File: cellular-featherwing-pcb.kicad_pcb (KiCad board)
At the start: 2 copper layers, 54 x 27 mm, 69 parts, among them J1 SIM8060-6-0-14-00-A, J2 TSM-116-01-L-SV, J3 TSM-112-01-L-SV, J4 U.FL-R-SMT, U1 BG96, U2 TPS63020QDSJTQ1, U3 TXB0108DQSR, U4 MAX8868EUK30+T

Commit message: Small updates
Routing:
- net (no net): track 13.9 -> 0.00 mm
- net Net-(C6-Pad1): track 0.00 -> 8.50 mm
- net Net-(C1-Pad1): track 0.00 -> 6.68 mm
- net Net-(R1-Pad2): track 0.00 -> 4.43 mm
- net GPS_ANT: track 3.97 -> 0.00 mm
- net VIN: track 0.00 -> 2.40 mm
- net Net-(C4-Pad1): track 0.00 -> 1.46 mm
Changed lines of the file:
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@@
     (property "Sheetname" "")
     (attr through_hole)
-    (fp_text reference "J2" (at -17.145 4.825) (layer "B.SilkS")
+    (fp_text reference "J2" (at -17.145 4.825) (layer "B.SilkS") hide
       (effects (font (size 1 1) (thickness 0.15)) (justify mirror))
     )
-    (fp_text value "TSM-116-01-L-SV" (at -6.35 -4.805) (layer "B.Fab")
+    (fp_text value "TSM-116-01-L-SV" (at -6.35 -4.805) (layer "B.Fab") hide
       (effects (font (size 1 1) (thickness 0.15)) (justify mirror))
     )
@@
     (property "Sheetname" "")
     (attr through_hole)
-    (fp_text reference "U4" (at 0.032 2.2064 90) (layer "B.SilkS")
+    (fp_text reference "U4" (at 0.032 2.2064 90) (layer "B.SilkS") hide
       (effects (font (size 0.64 0.64) (thickness 0.15)) (justify mirror))
     )
-    (fp_text value "MAX8868EUK30+T" (at 4.5024 -2.1936 90) (layer "B.Fab")
+    (fp_text value "MAX8868EUK30+T" (at 4.5024 -2.1936 90) (layer "B.Fab") hide
       (effects (font (size 0.64 0.64) (thickness 0.15)) (justify mirror))
     )
@@
     (property "Sheetname" "")
     (attr through_hole)
-    (fp_text reference "J3" (at -12.065 4.825) (layer "B.SilkS")
+    (fp_text reference "J3" (at -12.065 4.825) (layer "B.SilkS") hide
       (effects (font (size 1 1) (thickness 0.15)) (justify mirror))
     )
-    (fp_text value "TSM-112-01-L-SV" (at -1.27 -4.805) (layer "B.Fab")
+    (fp_text value "TSM-112-01-L-SV" (at -1.27 -4.805) (layer "B.Fab") hide
       (effects (font (size 1 1) (thickness 0.15)) (justify mirror))
     )
@@
   )
   (gr_rect locked (start 121 108) (end 175 81) (layer "Edge.Cuts") (width 0.1) (fill none))
-  (segment (start 163.0875 104.87) (end 162.0625 104.87) (width 0.25) (layer "F.Cu") (net 0))
-  (segment (start 167.95 107.3) (end 162.3925 107.3) (width 0.25) (layer "F.Cu") (net 0))
-  (segment (start 167.8875 104.9) (end 168.8875 104.9) (width 0.25) (layer "F.Cu") (net 0))
-  (segment (start 162.0625 104.87) (end 161.7875 105.145) (width 0.25) (layer "F.Cu") (net 0))
-  (segment (start 168.8875 106.3625) (end 167.95 107.3) (width 0.25) (layer "F.Cu") (net 0))
-  (segment (start 168.8875 104.9) (end 169.8875 104.9) (width 0.25) (layer "F.Cu") (net 0))
-  (segment (start 169.8875 104.9) (end 171.2 104.9) (width 0.25) (layer "F.Cu") (net 0))
-  (segment (start 162.3925 107.3) (end 161.7875 106.695) (width 0.25) (layer "F.Cu") (net 0))
-  (segment (start 166.9175 104.9) (end 167.8875 104.9) (width 0.25) (layer "F.Cu") (net 0))
-  (segment (start 168.8875 105.87) (end 168.8875 106.3625) (width 0.25) (layer "F.Cu") (net 0))
   (segment (start 170.78 97.95) (end 170.78 99.385) (width 0.2) (layer "B.Cu") (net 16))
   (segment (start 170.78 99.385) (end 170.8 99.405) (width 0.2) (layer "B.Cu") (net 16))
@@
   (segment (start 134.38 98.76) (end 134.38 97.205) (width 0.25) (layer "F.Cu") (net 73))
   (segment (start 134.38 97.205) (end 134.375 97.2) (width 0.25) (layer "F.Cu") (net 73))
-  (segment (start 165 104.8825) (end 165.0175 104.9) (width 0.25) (layer "F.Cu") (net 77))
-  (segment (start 165 101.88) (end 165 104.8825) (width 0.25) (layer "F.Cu") (net 77))
-  (segment (start 165.0175 104.9) (end 165.9575 104.9) (width 0.25) (layer "F.Cu") (net 77))
   (segment (start 169.35 87.45) (end 170.29 87.45) (width 0.25) (layer "F.Cu") (net 79))
   (segment (start 166.33 87.45) (end 169.35 87.45) (width 0.25) (layer "F.Cu") (net 79))
+  (segment (start 157.105 92.425) (end 156.95 92.27) (width 0.25) (layer "B.Cu") (net 81))
+  (segment (start 156.95 92.27) (end 155.8925 92.27) (width 0.25) (layer "B.Cu") (net 81))
+  (segment (start 155.6625 93.5375) (end 155.6625 92.5) (width 0.25) (layer "B.Cu") (net 81))
+  (segment (start 154.51 94) (end 155.2 94) (width 0.25) (layer "B.Cu") (net 81))
+  (segment (start 155.8925 92.27) (end 155.6625 92.5) (width 0.25) (layer "B.Cu") (net 81))
+  (segment (start 158.25 92.425) (end 157.105 92.425) (width 0.25) (layer "B.Cu") (net 81))
+  (segment (start 155.2 94) (end 155.6625 93.5375) (width 0.25) (layer "B.Cu") (net 81))
+  (segment (start 159.8 92.425) (end 158.25 92.425) (width 0.25) (layer "B.Cu") (net 81))
+  (segment (start 164.3875 90.7) (end 164.72 90.7) (width 0.25) (layer "B.Cu") (net 82))
+  (segment (start 164.72 90.7) (end 165.52 89.9) (width 0.25) (layer "B.Cu") (net 82))
+  (segment (start 167.75 92.425) (end 166.2 92.425) (width 0.25) (layer "B.Cu") (net 83))
+  (segment (start 164.3875 92.7) (end 164.3875 92.2) (width 0.25) (layer "B.Cu") (net 83))
+  (segment (start 169.3 92.425) (end 167.75 92.425) (width 0.25) (layer "B.Cu") (net 83))
+  (segment (start 164.3875 92.2) (end 165.975 92.2) (width 0.25) (layer "B.Cu") (net 83))
+  (segment (start 169.61 92.115) (end 169.3 92.425) (width 0.25) (layer "B.Cu") (net 83))
+  (segment (start 170.8875 92.425) (end 169.3 92.425) (width 0.25) (layer "B.Cu") (net 83))
+  (segment (start 169.61 91.15) (end 169.61 92.115) (width 0.25) (layer "B.Cu") (net 83))
+  (segment (start 165.975 92.2) (end 166.2 92.425) (width 0.25) (layer "B.Cu") (net 83))
   (segment (start 172.25 86.4625) (end 172.25 85.0875) (width 0.25) (layer "F.Cu") (net 84))
   (segment (start 172.25 87.45) (end 172.25 86.4625) (width 0.25) (layer "F.Cu") (net 84))
@@
   (segment (start 127.88 97.345) (end 128.025 97.2) (width 0.25) (layer "F.Cu") (net 86))
   (segment (start 127.88 99.26) (end 127.88 97.345) (width 0.25) (layer "F.Cu") (net 86))
+  (segment (start 137.55 91.8) (end 139.95 91.8) (width 0.25) (layer "B.Cu") (net 87))
   (segment (start 133.08 98.76) (end 131.88 98.76) (width 0.25) (layer "F.Cu") (net 88))
   (segment (start 131.85 97.215) (end 131.835 97.2) (width 0.25) (layer "F.Cu") (net 88))
@@
   (segment (start 169.85 101.895) (end 168.515 101.895) (width 0.2) (layer "B.Cu") (net 90))
   (segment (start 168.515 101.895) (end 168.5 101.88) (width 0.2) (layer "B.Cu") (net 90))
+  (segment (start 168.59 91.15) (end 167.65 91.15) (width 0.25) (layer "B.Cu") (net 91))
+  (segment (start 167.65 91.15) (end 167.6 91.2) (width 0.25) (layer "B.Cu") (net 91))
+  (segment (start 165.5 91.2) (end 167.6 91.2) (width 0.25) (layer "B.Cu") (net 91))
+  (segment (start 165 91.7) (end 165.5 91.2) (width 0.25) (layer "B.Cu") (net 91))
+  (segment (start 164.3875 91.7) (end 165 91.7) (width 0.25) (layer "B.Cu") (net 91))
   (segment (start 161.5875 93.2) (end 161.5875 93.7) (width 0.2) (layer "B.Cu") (net 94))
   (zone (net 16) (net_name "GND") (layer "F.Cu") (hatch edge 0.508)

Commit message: Updates from Javier
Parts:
- removed C30, C31, C33: 4.7uF, Capacitor_SMD:C_0402_1005Metric
- removed U4: MAX8868EUK30+T, MAX8868EUK30_:SOT95P280X145-5N
- moved TP12 12.1 mm to (152.9, 101.4)
- moved TP6 10.2 mm to (139.1, 95.1)
- moved TP5 4.91 mm to (141.6, 93.5)
- moved TP4 2.34 mm to (145.5, 92.6)
- moved TP8 1.69 mm to (139.2, 97.4)
- moved C34 0.53 mm to (144.1, 93.6)
- moved TP9 0.43 mm to (159.5, 89.0)
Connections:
- U1 pad 102: GND -> (no net)
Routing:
- net Net-(U1-Pad11): track 0.00 -> 73.6 mm
- net VDD: track 0.00 -> 62.5 mm, vias 0 -> 1
- net SIM_VDD: track 1.56 -> 62.4 mm, vias 0 -> 3
- net SIM_CLK: track 0.00 -> 40.7 mm
- net SIM_DATA: track 0.00 -> 35.6 mm
- net VMODEM: track 1.47 -> 36.7 mm, vias 0 -> 2
- net SIM_RST: track 0.00 -> 32.2 mm
- net GND: track 2.95 -> 32.6 mm, vias 0 -> 18
- net Net-(C16-Pad1): track 2.12 -> 27.3 mm, vias 0 -> 2
- net GSM_RXD: track 0.00 -> 24.7 mm
- net ENABLE: track 0.00 -> 24.4 mm
- net GSM_TXD: track 0.00 -> 20.3 mm
- net RI: track 0.00 -> 19.0 mm, vias 0 -> 1
- net DCD: track 0.00 -> 18.7 mm, vias 0 -> 1
- net GSM_STATUS_INT: track 0.00 -> 17.6 mm, vias 0 -> 1
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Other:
- board size 54 x 27 mm -> 54 x 32 mm

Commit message: Updated board from javier
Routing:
- net GND: vias 18 -> 19
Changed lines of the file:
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@@
     (fp_line (start -1.5 2) (end 1.5 2) (layer "B.Fab") (width 0.127))
     (fp_circle (center -2.2 1.5) (end -2.1 1.5) (layer "B.Fab") (width 0.2) (fill none))
-    (pad "1" smd oval locked (at -1.4 1.5 180) (size 0.6 0.24) (layers "B.Cu" "B.Paste")
+    (pad "1" smd oval (at -1.4 1.5 180) (size 0.6 0.24) (layers "B.Cu" "B.Paste")
       (net 82 "Net-(C4-Pad1)") (pinfunction "VINA") (pintype "input"))
-    (pad "2" smd oval locked (at -1.4 1 180) (size 0.6 0.24) (layers "B.Cu" "B.Paste")
+    (pad "2" smd oval (at -1.4 1 180) (size 0.6 0.24) (layers "B.Cu" "B.Paste")
       (net 16 "GND") (pinfunction "GND") (pintype "power_in"))
-    (pad "3" smd oval locked (at -1.4 0.5 180) (size 0.6 0.24) (layers "B.Cu" "B.Paste")
+    (pad "3" smd oval (at -1.4 0.5 180) (size 0.6 0.24) (layers "B.Cu" "B.Paste")
       (net 90 "Net-(R1-Pad2)") (pinfunction "FB") (pintype "input"))
-    (pad "4" smd oval locked (at -1.4 0 180) (size 0.6 0.24) (layers "B.Cu" "B.Paste")
+    (pad "4" smd oval (at -1.4 0 180) (size 0.6 0.24) (layers "B.Cu" "B.Paste")
       (net 83 "Net-(C6-Pad1)") (pinfunction "VOUT_4") (pintype "output"))
-    (pad "5" smd oval locked (at -1.4 -0.5 180) (size 0.6 0.24) (layers "B.Cu" "B.Paste")
+    (pad "5" smd oval (at -1.4 -0.5 180) (size 0.6 0.24) (layers "B.Cu" "B.Paste")
       (net 83 "Net-(C6-Pad1)") (pinfunction "VOUT_5") (pintype "output"))
-    (pad "6" smd oval locked (at -1.4 -1 180) (size 0.6 0.24) (layers "B.Cu" "B.Paste")
+    (pad "6" smd oval (at -1.4 -1 180) (size 0.6 0.24) (layers "B.Cu" "B.Paste")
       (net 94 "/L1_1") (pinfunction "L2_6") (pintype "passive"))
-    (pad "7" smd oval locked (at -1.4 -1.5 180) (size 0.6 0.24) (layers "B.Cu" "B.Paste")
+    (pad "7" smd oval (at -1.4 -1.5 180) (size 0.6 0.24) (layers "B.Cu" "B.Paste")
       (net 94 "/L1_1") (pinfunction "L2_7") (pintype "passive"))
-    (pad "8" smd oval locked (at 1.4 -1.5 180) (size 0.6 0.24) (layers "B.Cu" "B.Paste")
+    (pad "8" smd oval (at 1.4 -1.5 180) (size 0.6 0.24) (layers "B.Cu" "B.Paste")
       (net 93 "/L1_2") (pinfunction "L1_8") (pintype "passive"))
-    (pad "9" smd oval locked (at 1.4 -1 180) (size 0.6 0.24) (layers "B.Cu" "B.Paste")
+    (pad "9" smd oval (at 1.4 -1 180) (size 0.6 0.24) (layers "B.Cu" "B.Paste")
       (net 93 "/L1_2") (pinfunction "L1_9") (pintype "passive"))
-    (pad "10" smd oval locked (at 1.4 -0.5 180) (size 0.6 0.24) (layers "B.Cu" "B.Paste")
+    (pad "10" smd oval (at 1.4 -0.5 180) (size 0.6 0.24) (layers "B.Cu" "B.Paste")
       (net 81 "Net-(C1-Pad1)") (pinfunction "VIN_10") (pintype "input"))
-    (pad "11" smd oval locked (at 1.4 0 180) (size 0.6 0.24) (layers "B.Cu" "B.Paste")
+    (pad "11" smd oval (at 1.4 0 180) (size 0.6 0.24) (layers "B.Cu" "B.Paste")
       (net 81 "Net-(C1-Pad1)") (pinfunction "VIN_11") (pintype "input"))
-    (pad "12" smd oval locked (at 1.4 0.5 180) (size 0.6 0.24) (layers "B.Cu" "B.Paste")
+    (pad "12" smd oval (at 1.4 0.5 180) (size 0.6 0.24) (layers "B.Cu" "B.Paste")
       (net 47 "ENABLE") (pinfunction "EN") (pintype "input"))
-    (pad "13" smd oval locked (at 1.4 1 180) (size 0.6 0.24) (layers "B.Cu" "B.Paste")
+    (pad "13" smd oval (at 1.4 1 180) (size 0.6 0.24) (layers "B.Cu" "B.Paste")
       (net 81 "Net-(C1-Pad1)") (pinfunction "PS/SYNC") (pintype "input"))
-    (pad "14" smd oval locked (at 1.4 1.5 180) (size 0.6 0.24) (layers "B.Cu" "B.Paste")
+    (pad "14" smd oval (at 1.4 1.5 180) (size 0.6 0.24) (layers "B.Cu" "B.Paste")
       (net 19 "unconnected-(U2-Pad14)") (pinfunction "PG") (pintype "output"))
-    (pad "15" smd custom locked (at 0 0 180) (size 1.5 2.8) (layers "B.Cu")
+    (pad "15" smd custom (at 0 0 180) (size 1.5 2.8) (layers "B.Cu")
       (net 16 "GND") (pinfunction "PGND") (pintype "power_in") (zone_connect 0)
       (options (clearance outline) (anchor rect))
@@
           ) (width 0.01) (fill yes))
       ))
-    (pad "16" thru_hole circle locked (at -0.5 1 180) (size 0.3 0.3) (drill 0.2) (layers *.Cu *.Mask))
-    (pad "17" thru_hole circle locked (at 0 1 180) (size 0.3 0.3) (drill 0.2) (layers *.Cu *.Mask))
-    (pad "18" thru_hole circle locked (at 0.5 1 180) (size 0.3 0.3) (drill 0.2) (layers *.Cu *.Mask))
-    (pad "19" thru_hole circle locked (at -0.5 0.5 180) (size 0.3 0.3) (drill 0.2) (layers *.Cu *.Mask))
-    (pad "20" thru_hole circle locked (at 0 0.5 180) (size 0.3 0.3) (drill 0.2) (layers *.Cu *.Mask))
-    (pad "21" thru_hole circle locked (at 0.5 0.5 180) (size 0.3 0.3) (drill 0.2) (layers *.Cu *.Mask))
-    (pad "22" thru_hole circle locked (at -0.5 0 180) (size 0.3 0.3) (drill 0.2) (layers *.Cu *.Mask))
-    (pad "23" thru_hole circle locked (at 0 0 180) (size 0.3 0.3) (drill 0.2) (layers *.Cu *.Mask))
-    (pad "24" thru_hole circle locked (at 0.5 0 180) (size 0.3 0.3) (drill 0.2) (layers *.Cu *.Mask))
-    (pad "25" thru_hole circle locked (at -0.5 -0.5 180) (size 0.3 0.3) (drill 0.2) (layers *.Cu *.Mask))
-    (pad "26" thru_hole circle locked (at 0 -0.5 180) (size 0.3 0.3) (drill 0.2) (layers *.Cu *.Mask))
-    (pad "27" thru_hole circle locked (at 0.5 -0.5 180) (size 0.3 0.3) (drill 0.2) (layers *.Cu *.Mask))
-    (pad "28" thru_hole circle locked (at -0.5 -1 180) (size 0.3 0.3) (drill 0.2) (layers *.Cu *.Mask))
-    (pad "29" thru_hole circle locked (at 0 -1 180) (size 0.3 0.3) (drill 0.2) (layers *.Cu *.Mask))
-    (pad "30" thru_hole circle locked (at 0.5 -1 180) (size 0.3 0.3) (drill 0.2) (layers *.Cu *.Mask))
   )
   (footprint "TestPoint:TestPoint_Pad_D1.0mm" (layer "B.Cu")
@@
   (via (at 132.969 100.5078) (size 0.8) (drill 0.4) (layers "F.Cu" "B.Cu") (free) (net 16))
   (via (at 151.7396 92.8624) (size 0.8) (drill 0.4) (layers "F.Cu" "B.Cu") (free) (net 16))
+  (via (at 162.941 91.8718) (size 0.8) (drill 0.4) (layers "F.Cu" "B.Cu") (net 16))
   (via (at 168.021 96.52) (size 0.8) (drill 0.4) (layers "F.Cu" "B.Cu") (free) (net 16))
   (via (at 138.9888 93.345) (size 0.8) (drill 0.4) (layers "F.Cu" "B.Cu") (net 16))
@@
   (via (at 161.0614 88.7222) (size 0.8) (drill 0.4) (layers "F.Cu" "B.Cu") (free) (net 81))
   (via (at 159.0548 91.2368) (size 0.8) (drill 0.4) (layers "F.Cu" "B.Cu") (free) (net 81))
-  (segment (start 161.9057 91.2) (end 161.9425 91.2368) (width 0.1) (layer "B.Cu") (net 81))
   (segment (start 157.105 92.425) (end 156.95 92.27) (width 0.2) (layer "B.Cu") (net 81))
   (segment (start 160.9578 92.2) (end 159.9946 91.2368) (width 0.2) (layer "B.Cu") (net 81))

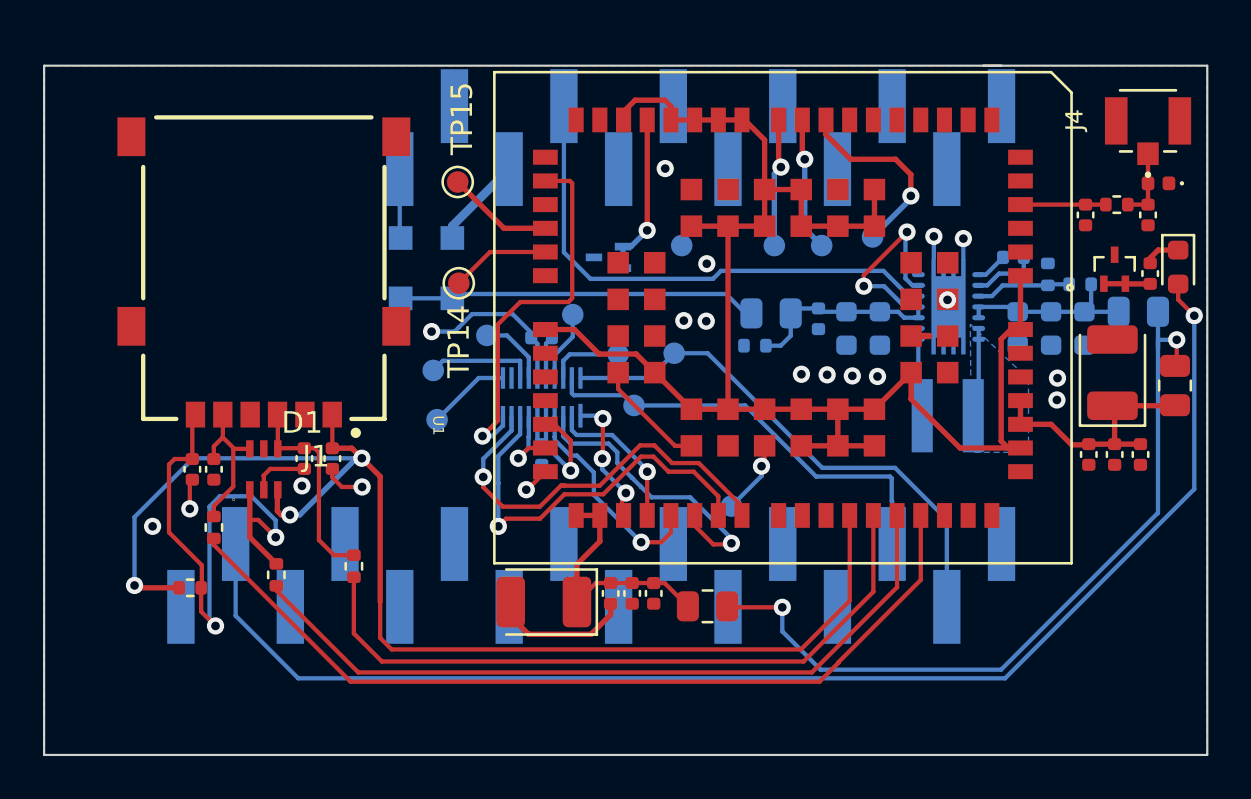
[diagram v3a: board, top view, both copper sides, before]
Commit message: All items routed
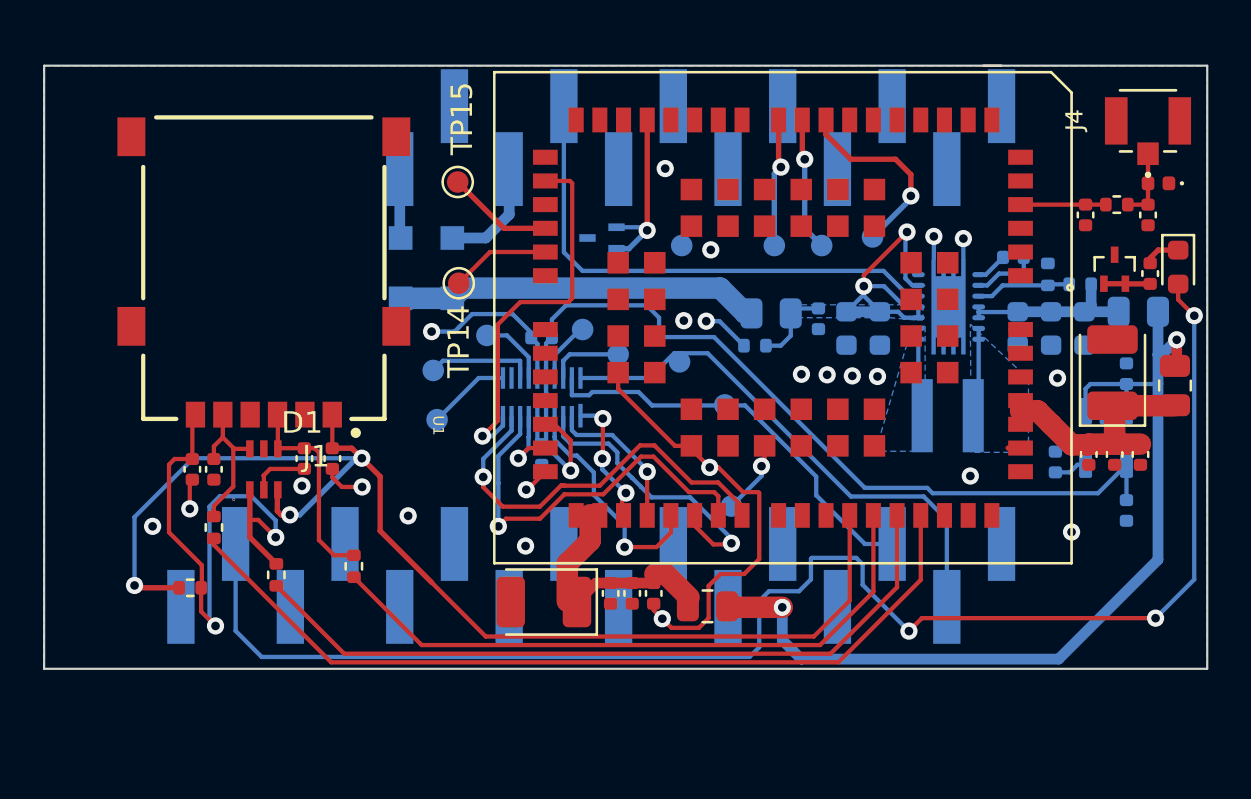
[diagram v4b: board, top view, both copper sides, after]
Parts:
- added C30: 4.7uF, Capacitor_SMD:C_0402_1005Metric, B.Cu at (171.2, 95.3)
- added C31: 4.7uF, Capacitor_SMD:C_0402_1005Metric, B.Cu at (171.2, 101.7)
- added C33: 4.7uF, Capacitor_SMD:C_0402_1005Metric, B.Cu at (167.9, 99.4)
- added U4: MAX8868EUK30+T, MAX8868EUK30_:SOT95P280X145-5N, B.Cu at (170.3, 98.3)
- moved TP1 4.21 mm to (152.6, 96.8)
- moved VT4 0.95 mm to (146.9, 89.0)
- moved TP4 0.83 mm to (146.0, 93.2)
- moved TP2 0.47 mm to (150.5, 94.8)
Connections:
- U1 pad 102: (no net) -> GND
- U1 pad 11: Net-(U1-Pad11) -> (no net)
- U1 pad 12: Net-(U1-Pad11) -> (no net)
- U1 pad 13: Net-(U1-Pad11) -> (no net)
- U1 pad 14: Net-(U1-Pad11) -> (no net)
- U1 pad 16: Net-(U1-Pad11) -> (no net)
- U1 pad 25: Net-(U1-Pad11) -> (no net)
- U1 pad 27: GPS_TXD -> unconnected-(U1-Pad27)
- U1 pad 28: GPS_RXD -> unconnected-(U1-Pad28)
- U1 pad 51: Net-(U1-Pad11) -> (no net)
- U1 pad 56: Net-(U1-Pad11) -> (no net)
- U1 pad 57: Net-(U1-Pad11) -> (no net)
- U1 pad 63: Net-(U1-Pad11) -> (no net)
- U1 pad 65: Net-(U1-Pad11) -> (no net)
- U1 pad 66: Net-(U1-Pad11) -> (no net)
- U1 pad 76: Net-(U1-Pad11) -> (no net)
- U1 pad 77: Net-(U1-Pad11) -> (no net)
- U1 pad 78: Net-(U1-Pad11) -> (no net)
- U1 pad 83: Net-(U1-Pad11) -> (no net)
- U1 pad 84: Net-(U1-Pad11) -> (no net)
- U1 pad 85: Net-(U1-Pad11) -> (no net)
- U1 pad 86: Net-(U1-Pad11) -> (no net)
- U1 pad 87: Net-(U1-Pad11) -> (no net)
- U1 pad 88: Net-(U1-Pad11) -> (no net)
- U1 pad 92: Net-(U1-Pad11) -> (no net)
- U1 pad 93: Net-(U1-Pad11) -> (no net)
- U1 pad 94: Net-(U1-Pad11) -> (no net)
- U1 pad 95: Net-(U1-Pad11) -> (no net)
- U1 pad 96: Net-(U1-Pad11) -> (no net)
- U1 pad 97: Net-(U1-Pad11) -> (no net)
- U1 pad 98: Net-(U1-Pad11) -> (no net)
- U1 pad 99: Net-(U1-Pad11) -> (no net)
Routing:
- net Net-(U1-Pad11): track 73.6 -> 0.00 mm
- net 3V3: track 1.99 -> 37.0 mm
- net GND: track 32.6 -> 43.1 mm, vias 19 -> 23
- net VDD: track 62.5 -> 69.7 mm, vias 1 -> 3
- net VMODEM: track 36.7 -> 43.5 mm
- net SIM_VDD: track 62.4 -> 59.0 mm
- net SIM_RST: track 32.2 -> 30.0 mm
- net Net-(C1-Pad1): track 18.6 -> 20.4 mm
- net Net-(C33-Pad1): track 0.00 -> 1.55 mm
- net (no net): track 0.00 -> 1.41 mm
- net GSM_TXD: track 20.3 -> 19.2 mm
- net 5V: track 4.29 -> 5.20 mm
- net SIM_DATA: track 35.6 -> 34.7 mm
- net ON_PIN: track 7.56 -> 8.39 mm
- net CTS: track 10.0 -> 10.8 mm
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- added copper zone on B.Cu, net /L1_2
- added copper zone on B.Cu, net Net-(C1-Pad1)
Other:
- board size 54 x 32 mm -> 54 x 28 mm
